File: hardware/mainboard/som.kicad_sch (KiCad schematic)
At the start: 15 parts, among them SW1 SW_DIP_x04, U1 CP3225-100.000-3.3-25-X-T-TR, U2 AX3HAF1-135.0000T

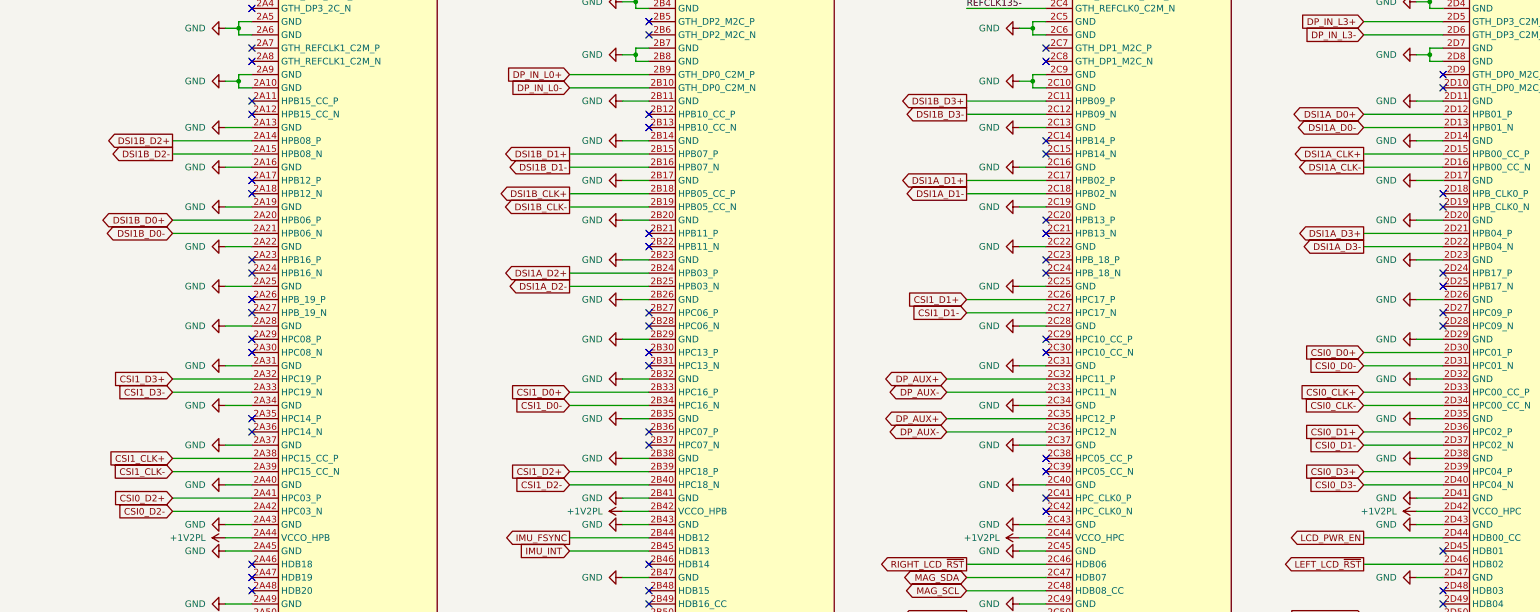
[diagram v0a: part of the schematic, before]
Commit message: First pass high-speed routing
Signed-off-by: gatecat <gatecat@ds0.me>
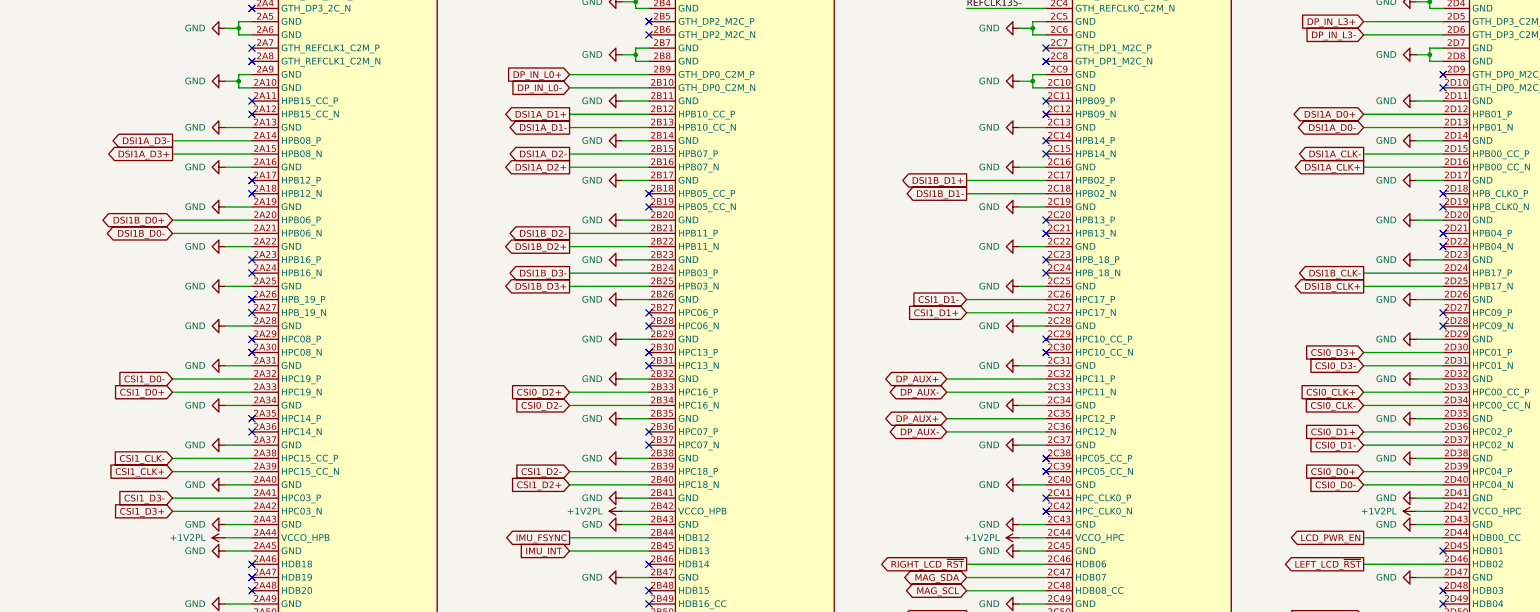
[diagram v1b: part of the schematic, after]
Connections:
- net CSI0_D0+: now also SOM1.2D39 (HPC04_P); no longer SOM1.2D30 (HPC01_P)
- net CSI0_D0-: now also SOM1.2D40 (HPC04_N); no longer SOM1.2D31 (HPC01_N)
- net CSI0_D2+: now also SOM1.2B33 (HPC16_P); no longer SOM1.2A41 (HPC03_P)
- net CSI0_D2-: now also SOM1.2B34 (HPC16_N); no longer SOM1.2A42 (HPC03_N)
- net CSI0_D3+: now also SOM1.2D30 (HPC01_P); no longer SOM1.2D39 (HPC04_P)
- net CSI0_D3-: now also SOM1.2D31 (HPC01_N); no longer SOM1.2D40 (HPC04_N)
- net CSI1_CLK+: now also SOM1.2A39 (HPC15_CC_N); no longer SOM1.2A38 (HPC15_CC_P)
- net CSI1_CLK-: now also SOM1.2A38 (HPC15_CC_P); no longer SOM1.2A39 (HPC15_CC_N)
- net CSI1_D0+: now also SOM1.2A33 (HPC19_N); no longer SOM1.2B33 (HPC16_P)
- net CSI1_D0-: now also SOM1.2A32 (HPC19_P); no longer SOM1.2B34 (HPC16_N)
- net CSI1_D1+: now also SOM1.2C27 (HPC17_N); no longer SOM1.2C26 (HPC17_P)
- net CSI1_D1-: now also SOM1.2C26 (HPC17_P); no longer SOM1.2C27 (HPC17_N)
- net CSI1_D2+: now also SOM1.2B40 (HPC18_N); no longer SOM1.2B39 (HPC18_P)
- net CSI1_D2-: now also SOM1.2B39 (HPC18_P); no longer SOM1.2B40 (HPC18_N)
- net CSI1_D3+: now also SOM1.2A42 (HPC03_N); no longer SOM1.2A32 (HPC19_P)
- net CSI1_D3-: now also SOM1.2A41 (HPC03_P); no longer SOM1.2A33 (HPC19_N)
- net DSI1A_CLK+: now also SOM1.2D16 (HPB00_CC_N); no longer SOM1.2D15 (HPB00_CC_P)
- net DSI1A_CLK-: now also SOM1.2D15 (HPB00_CC_P); no longer SOM1.2D16 (HPB00_CC_N)
- net DSI1A_D1+: now also SOM1.2B12 (HPB10_CC_P); no longer SOM1.2C17 (HPB02_P)
- net DSI1A_D1-: now also SOM1.2B13 (HPB10_CC_N); no longer SOM1.2C18 (HPB02_N)
- net DSI1A_D2+: now also SOM1.2B16 (HPB07_N); no longer SOM1.2B24 (HPB03_P)
- net DSI1A_D2-: now also SOM1.2B15 (HPB07_P); no longer SOM1.2B25 (HPB03_N)
- net DSI1A_D3+: now also SOM1.2A15 (HPB08_N); no longer SOM1.2D21 (HPB04_P)
- net DSI1A_D3-: now also SOM1.2A14 (HPB08_P); no longer SOM1.2D22 (HPB04_N)
- net DSI1B_CLK+: now also SOM1.2D25 (HPB17_N); no longer SOM1.2B18 (HPB05_CC_P)
- net DSI1B_CLK-: now also SOM1.2D24 (HPB17_P); no longer SOM1.2B19 (HPB05_CC_N)
- net DSI1B_D1+: now also SOM1.2C17 (HPB02_P); no longer SOM1.2B15 (HPB07_P)
- net DSI1B_D1-: now also SOM1.2C18 (HPB02_N); no longer SOM1.2B16 (HPB07_N)
- net DSI1B_D2+: now also SOM1.2B22 (HPB11_N); no longer SOM1.2A14 (HPB08_P)
- net DSI1B_D2-: now also SOM1.2B21 (HPB11_P); no longer SOM1.2A15 (HPB08_N)
- net DSI1B_D3+: now also SOM1.2B25 (HPB03_N); no longer SOM1.2C11 (HPB09_P)
- net DSI1B_D3-: now also SOM1.2B24 (HPB03_P); no longer SOM1.2C12 (HPB09_N)

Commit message: Initial power routing
Signed-off-by: gatecat <gatecat@ds0.me>
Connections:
- net PL_LED2R: now also SOM1.2A58 (HDC21); no longer SOM1.2B52 (HDC12)
- net PL_LED4R: now also SOM1.2B52 (HDC12); no longer SOM1.2A58 (HDC21)

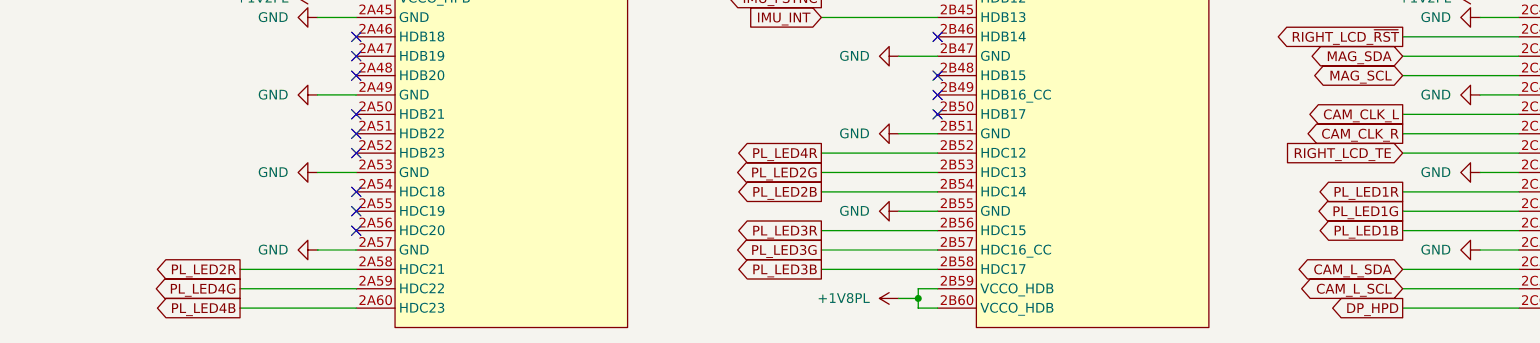
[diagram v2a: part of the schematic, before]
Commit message: Route and pinswap PL LEDs
Signed-off-by: gatecat <gatecat@ds0.me>
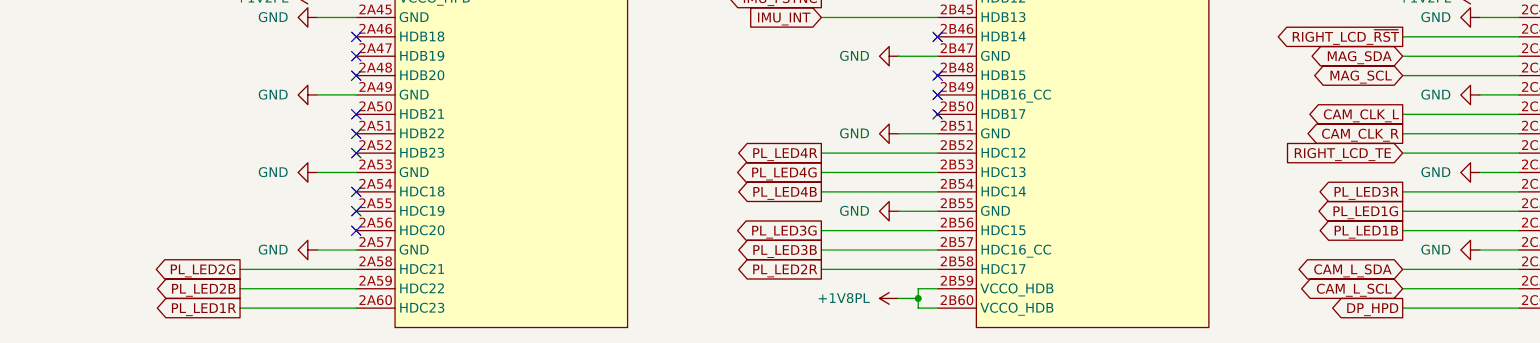
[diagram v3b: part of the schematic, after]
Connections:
- net PL_LED1R: now also SOM1.2A60 (HDC23); no longer SOM1.2C54 (HDC06)
- net PL_LED2B: now also SOM1.2A59 (HDC22); no longer SOM1.2B54 (HDC14)
- net PL_LED2G: now also SOM1.2A58 (HDC21); no longer SOM1.2B53 (HDC13)
- net PL_LED2R: now also SOM1.2B58 (HDC17); no longer SOM1.2A58 (HDC21)
- net PL_LED3B: now also SOM1.2B57 (HDC16_CC); no longer SOM1.2B58 (HDC17)
- net PL_LED3G: now also SOM1.2B56 (HDC15); no longer SOM1.2B57 (HDC16_CC)
- net PL_LED3R: now also SOM1.2C54 (HDC06); no longer SOM1.2B56 (HDC15)
- net PL_LED4B: now also SOM1.2B54 (HDC14); no longer SOM1.2A60 (HDC23)
- net PL_LED4G: now also SOM1.2B53 (HDC13); no longer SOM1.2A59 (HDC22)

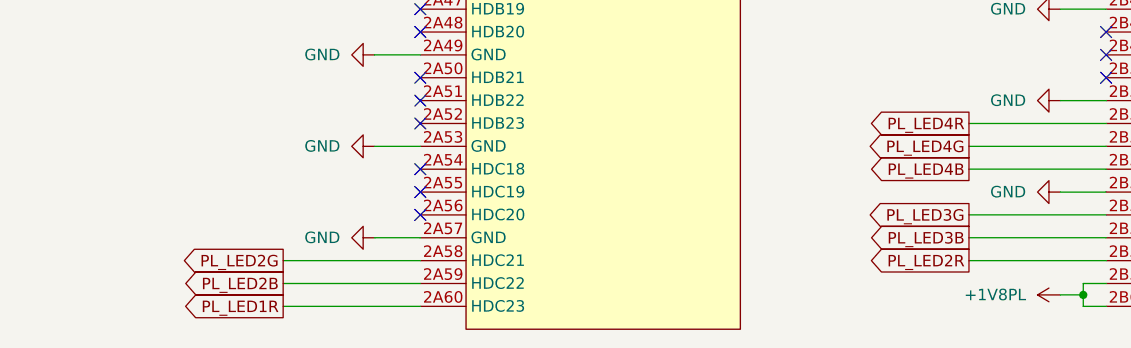
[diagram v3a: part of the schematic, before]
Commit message: Fixup Kria footprint
Signed-off-by: gatecat <gatecat@ds0.me>
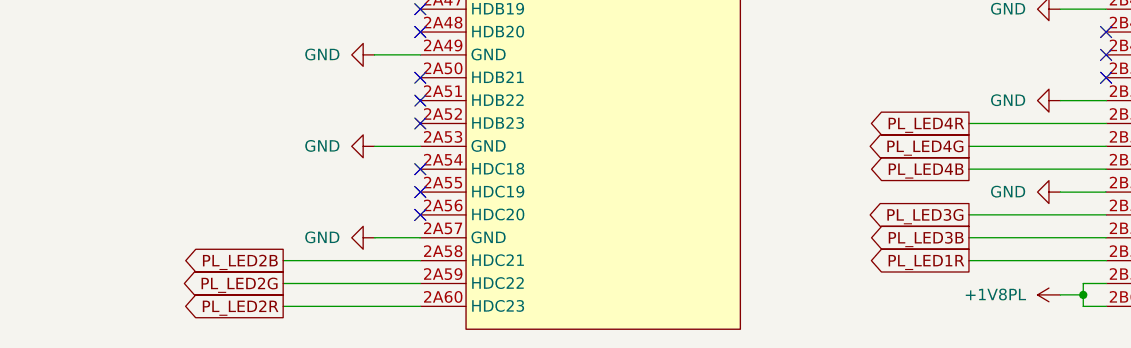
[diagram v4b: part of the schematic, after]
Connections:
- net PL_LED1R: now also SOM1.2B58 (HDC17); no longer SOM1.2A60 (HDC23)
- net PL_LED2B: now also SOM1.2A58 (HDC21); no longer SOM1.2A59 (HDC22)
- net PL_LED2G: now also SOM1.2A59 (HDC22); no longer SOM1.2A58 (HDC21)
- net PL_LED2R: now also SOM1.2A60 (HDC23); no longer SOM1.2B58 (HDC17)

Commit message: Rework LCD PWM setup
Signed-off-by: gatecat <gatecat@ds0.me>
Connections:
- net BL_PWM: now reaches SOM1.2A56 (HDC20)
- no-connect marks 126 -> 125
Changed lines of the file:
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@@
   (no_connect (at 306.07 312.42))
   (no_connect (at 229.87 302.26))
-  (no_connect (at 77.47 340.36))
   (no_connect (at 306.07 320.04))
   (no_connect (at 229.87 68.58))
@@
     (stroke (width 0) (type default) (color 0 0 0 0))
   )
+  (wire (pts (xy 62.23 340.36) (xy 77.47 340.36))
+    (stroke (width 0) (type default) (color 0 0 0 0))
+  )
   (wire (pts (xy 290.83 281.94) (xy 306.07 281.94))
     (stroke (width 0) (type default) (color 0 0 0 0))
@@
       (effects (font (size 1.27 1.27)) (justify right) hide)
     )
+  )
+  (global_label "BL_PWM" (shape output) (at 62.23 340.36 180) (fields_autoplaced)
+    (effects (font (size 1.27 1.27)) (justify right))
+    (property "Intersheet References" "${INTERSHEET_REFS}" (id 0) (at 52.3783 340.2806 0)
+      (effects (font (size 1.27 1.27)) (justify right) hide)
+    )

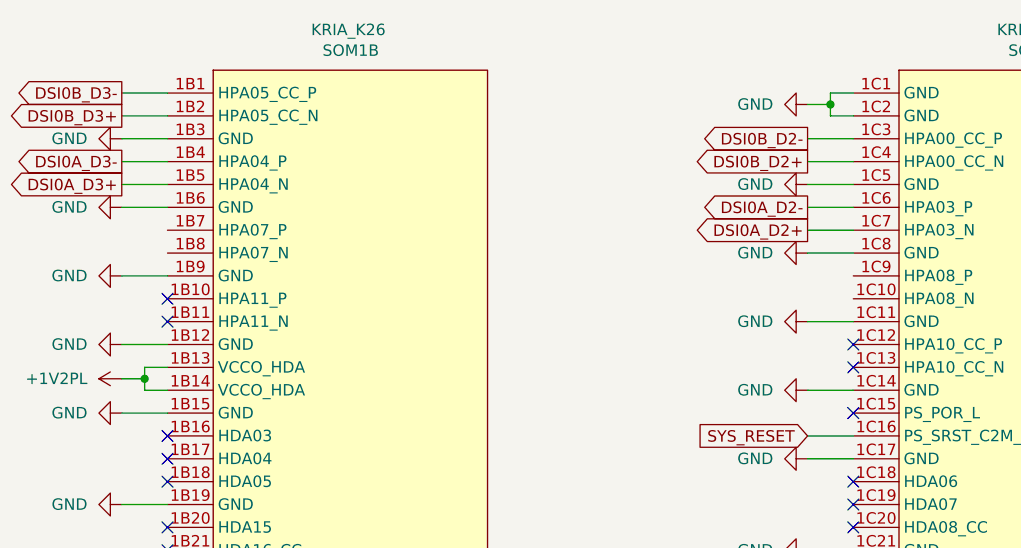
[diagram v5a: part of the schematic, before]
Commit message: Fix some ERC/DRC issues
Signed-off-by: gatecat <gatecat@ds0.me>
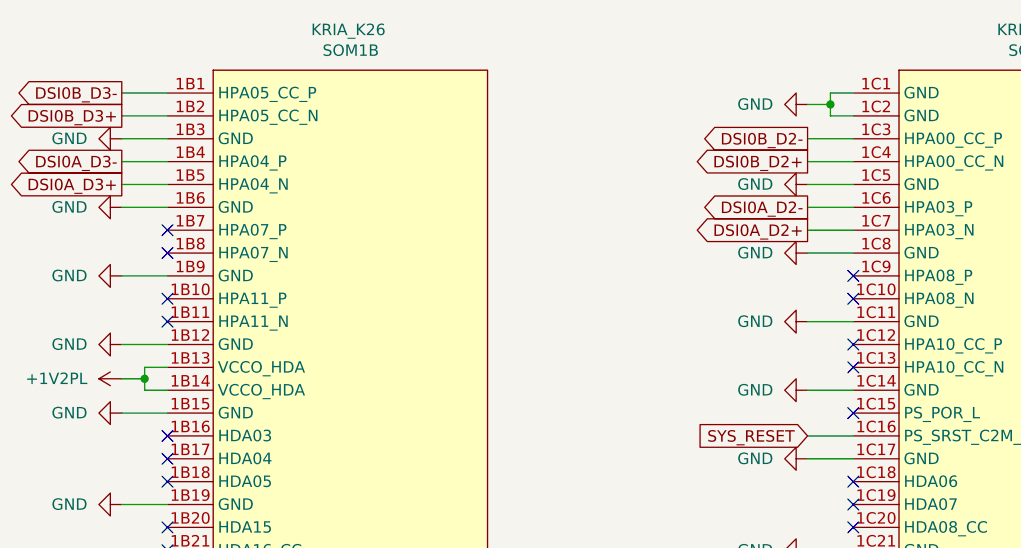
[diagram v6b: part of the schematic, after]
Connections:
- no-connect marks 125 -> 129
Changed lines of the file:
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@@
   (no_connect (at 77.47 106.68))
   (no_connect (at 77.47 317.5))
+  (no_connect (at 229.87 45.72))
   (no_connect (at 229.87 248.92))
   (no_connect (at 77.47 218.44))
@@
   (no_connect (at 77.47 266.7))
   (no_connect (at 229.87 215.9))
+  (no_connect (at 229.87 43.18))
   (no_connect (at 153.67 322.58))
   (no_connect (at 229.87 218.44))
@@
   (no_connect (at 153.67 325.12))
   (no_connect (at 153.67 147.32))
+  (no_connect (at 153.67 38.1))
   (no_connect (at 153.67 63.5))
+  (no_connect (at 153.67 40.64))
   (no_connect (at 430.53 151.13))
   (no_connect (at 77.47 129.54))
